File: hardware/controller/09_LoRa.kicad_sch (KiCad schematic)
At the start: 6 parts, among them J7 LoRa antenna U.FL, U70 Silicontra SX1262ZTR8-GC

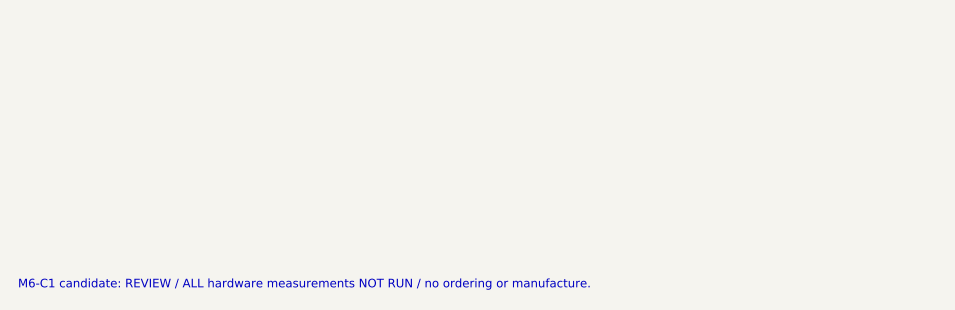
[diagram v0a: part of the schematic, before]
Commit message: M6-C1R1: protect pack identity input and review USB ESD topology
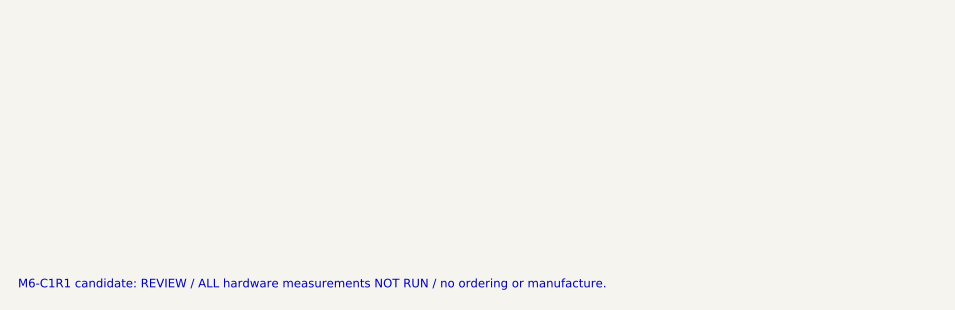
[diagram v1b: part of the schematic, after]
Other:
- note added: "M6-C1R1 candidate: REVIEW / ALL hardware measurements NOT RUN / no ordering or manufacture."
- note removed: "M6-C1 candidate: REVIEW / ALL hardware measurements NOT RUN / no ordering or manufacture."

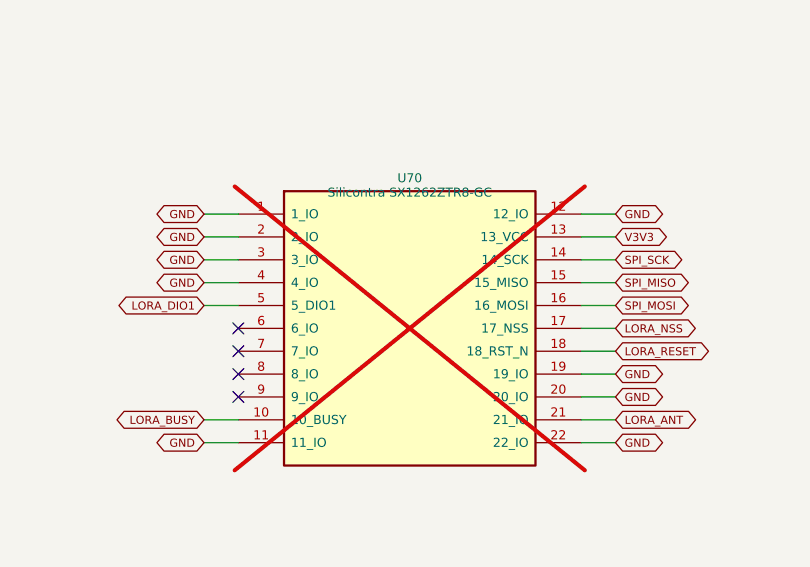
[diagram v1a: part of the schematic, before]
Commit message: M6-L1: close dual-band Silicontra footprint and RF feed review
Verify TR4/TR8 supplier aliases and all 22 nominal module terminals; retain
the common RF signal feed and Hirose lands. Remove a local ground-fill
intrusion in the full U.FL underbody keep-out and correct the module body
outline and unused DIO3 label.

Add explicit no-radio/433/868 assembly records, fail-disabled band/policy
fixtures, native-geometry mutations, tolerance RF calculations and fresh
standard-JLCPCB fabrication/assembly exports with source-bound manifests.

KiCad 10.0.6 ERC/DRC warnings/errors, unrouted and parity all zero. Preserve
704 pad assertions, 36 RF pins, 4096 enable cases, R1 protection/DFM tests,
46 host tests and strict C11 fixture. Physical qualification NOT_RUN.
Independent manufacturing review candidate only; no acceptance tag.
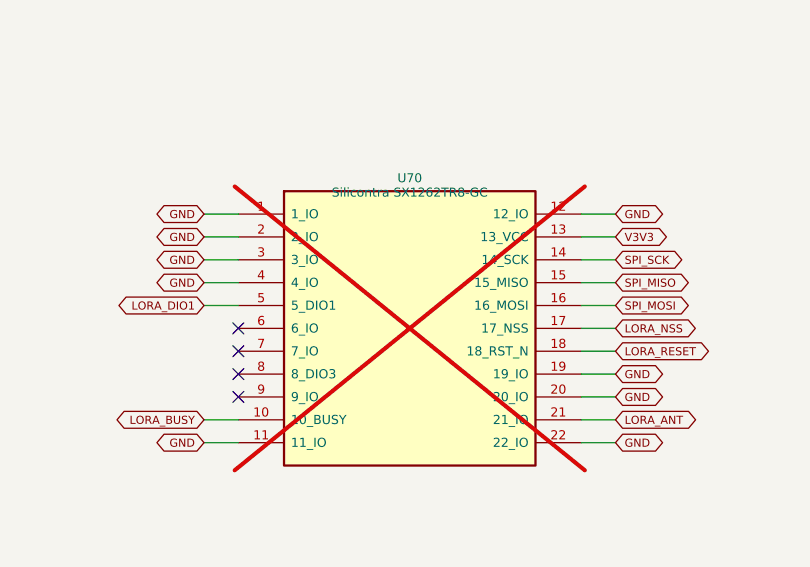
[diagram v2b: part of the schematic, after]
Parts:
- C70, C71, R70, R71: Population LORA_OPTION_OPEN -> LORA_OPTION
- J7: Engineering_Note Pin1 signal; duplicated pin2 ground. Underbody copper keepo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 -> M6-L1: Hirose U.FL-R-SMT-1(10), available cut tape MOQ1. Sa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; Population LORA_OPTION_OPEN -> LORA_OPTION
- U70: value Silicontra SX1262ZTR8-GC -> Silicontra SX1262TR8-GC; Engineering_Note OPTIONAL DNP: manufacturer ZTR8 vs distributor TR8 suffix n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 -> M6-L1: TR4/ZTR4 and TR8/ZTR8 supplier-linked manufacturer d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; MPN SX1262ZTR8-GC -> SX1262TR8-GC; Population LORA_OPTION_OPEN -> LORA_OPTION
